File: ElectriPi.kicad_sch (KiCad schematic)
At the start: 56 parts, among them IC2 TPS51397ARJER, J1 282837-2, J2 JST XH 01x02, J3 JST XH 01x02, J6 Raspberry_Pi_2_3, J8 JST XH 01x02, Q1 SiA471DJ, Q2 SiA430DJT, U1 LM74700, U2 COOLING

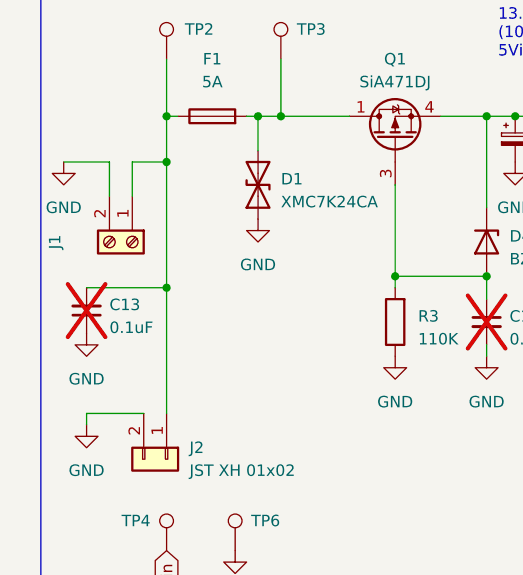
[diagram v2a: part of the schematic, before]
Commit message: Updated fuseholder to Keystone 3557 - low profile mini ATO fuses.
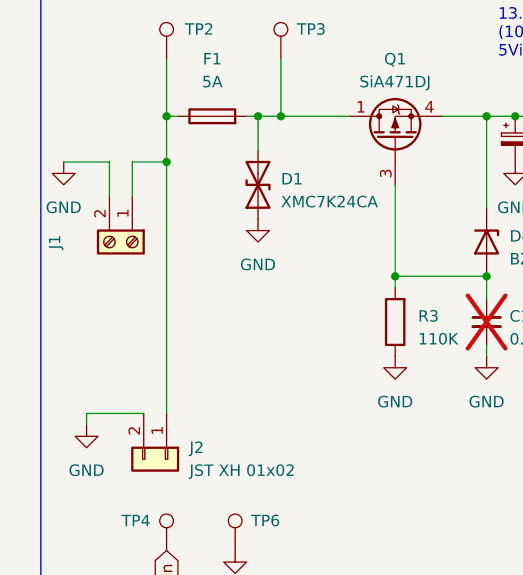
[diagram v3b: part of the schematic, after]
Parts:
- removed C13: 0.1uF, Capacitor_SMD:C_0402_1005Metric, symbol Device:C_Small
- F1: footprint Fuse:Fuse_Littelfuse-NANO2-451_453 -> Fuse:Fuseholder_Blade_Mini_Keystone_3557; DigiKey F1889-ND -> 36-3557-2-ND
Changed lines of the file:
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@@
   (junction (at 31.75 40.64) (diameter 0) (color 0 0 0 0)
-  )
-  (junction (at 31.75 59.69) (diameter 0) (color 0 0 0 0)
   )
   (junction (at 92.075 40.64) (diameter 0) (color 0 0 0 0)
@@
     (stroke (width 0) (type default))
   )
-  (wire (pts (xy 31.75 59.69) (xy 31.75 73.66))
-    (stroke (width 0) (type default))
-  )
   (wire (pts (xy 217.17 53.34) (xy 217.17 50.8))
     (stroke (width 0) (type default))
@@
     (stroke (width 0) (type default))
   )
-  (wire (pts (xy 22.86 59.69) (xy 31.75 59.69))
-    (stroke (width 0) (type default))
-  )
   (polyline (pts (xy 232.41 25.4) (xy 232.41 101.6))
     (stroke (width 0) (type default))
@@
     (stroke (width 0) (type default))
   )
-  (wire (pts (xy 31.75 45.72) (xy 31.75 59.69))
+  (wire (pts (xy 31.75 45.72) (xy 31.75 73.66))
     (stroke (width 0) (type default))
   )
@@
     )
   )
-  (symbol (lib_id "Device:C_Small") (at 22.86 62.23 180) (unit 1)
-    (in_bom yes) (on_board yes) (dnp yes) (fields_autoplaced)
-    (property "Reference" "C13" (at 25.4 61.5886 0)
-      (effects (font (size 1.27 1.27)) (justify right))
-    )
-    (property "Value" "0.1uF" (at 25.4 64.1286 0)
-      (effects (font (size 1.27 1.27)) (justify right))
-    )
-    (property "Footprint" "Capacitor_SMD:C_0402_1005Metric" (at 22.86 62.23 0)
-      (effects (font (size 1.27 1.27)) hide)
-    )
-    (property "Datasheet" "~" (at 22.86 62.23 0)
-      (effects (font (size 1.27 1.27)) hide)
-    )
-    (property "Mouser" "81-GRM155R62A104KE4J" (at 22.86 62.23 0)
-      (effects (font (size 1.27 1.27)) hide)
-    )
-    (property "LCSC" "C2193622" (at 22.86 62.23 0)
-      (effects (font (size 1.27 1.27)) hide)
-    )
-    (property "DigiKey" "490-GRM155R62A104KE14JTR-ND" (at 22.86 62.23 0)
-      (effects (font (size 1.27 1.27)) hide)
-    )
-    (pin "1")
-    (pin "2")
-    (instances
-      (project "ElectriPi"
-        (path "/e63e39d7-6ac0-4ffd-8aa3-1841a4541b55"
-          (reference "C13") (unit 1)
-        )
-      )
-    )
-  )
   (symbol (lib_id "power:PWR_FLAG") (at 217.17 138.43 0) (unit 1)
     (in_bom yes) (on_board yes) (dnp no) (fields_autoplaced)
@@
     )
   )
-  (symbol (lib_id "power:GND") (at 22.86 64.77 0) (unit 1)
-    (in_bom yes) (on_board yes) (dnp no) (fields_autoplaced)
-    (property "Reference" "#PWR043" (at 22.86 71.12 0)
-      (effects (font (size 1.27 1.27)) hide)
-    )
-    (property "Value" "GND" (at 22.86 69.85 0)
-      (effects (font (size 1.27 1.27)))
-    )
-    (property "Footprint" "" (at 22.86 64.77 0)
-      (effects (font (size 1.27 1.27)) hide)
-    )
-    (property "Datasheet" "" (at 22.86 64.77 0)
-      (effects (font (size 1.27 1.27)) hide)
-    )
-    (pin "1")
-    (instances
-      (project "ElectriPi"
-        (path "/e63e39d7-6ac0-4ffd-8aa3-1841a4541b55"
-          (reference "#PWR043") (unit 1)
-        )
-      )
-    )
-  )
   (symbol (lib_id "Connector:TestPoint") (at 39.37 88.9 0) (unit 1)
     (in_bom no) (on_board yes) (dnp no)
@@
       (effects (font (size 1.27 1.27)))
     )
-    (property "Footprint" "Fuse:Fuse_Littelfuse-NANO2-451_453" (at 36.83 42.418 90)
+    (property "Footprint" "Fuse:Fuseholder_Blade_Mini_Keystone_3557" (at 36.83 42.418 90)
       (effects (font (size 1.27 1.27)) hide)
     )
@@
       (effects (font (size 1.27 1.27)) hide)
     )
-    (property "DigiKey" "F1889-ND" (at 36.83 40.64 90)
-      (effects (font (size 1.27 1.27)) hide)
-    )
+    (property "DigiKey" "36-3557-2-ND" (at 36.83 40.64 90)
+      (effects (font (size 1.27 1.27)) hide)
+    )

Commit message: updated BOM, gerbers, and symbol fields (mouser and LCSC PNs updated, useless fields removed)
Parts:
- C3: ManfNum CL10A105KB8NNNC -> (none); Mouser (none) -> 187-CL10A105KB8NNNC; PCBway CL10A105KB8NNNC -> (none); abv.Footprint 0603 -> (none)
- D3, D5: ManfNum 19-213/Y2C-CQ2R2L/3T(CY) -> (none); Mouser (none) -> 604-APT1608SYCK; PCBway 19-213/Y2C-CQ2R2L/3T(CY) -> (none); abv.Footprint 0603 -> (none)
- F1: LCSC C108518 -> C352820; Mouser (none) -> 534-3557-2
- IC2: Arrow Part Number TPS51397ARJER -> (none); Arrow Price/Stock https://www.arrow.com/en/products/tps51397arjer/texas-instr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 -> (none); Height 1 -> (none); Manufacturer_Name Texas Instruments -> (none); Manufacturer_Part_Number TPS51397ARJER -> (none); Mouser (none) -> 595-TPS51397ARJER; Mouser Part Number 595-TPS51397ARJER -> (none); Mouser Price/Stock https://www.mouser.co.uk/ProductDetail/Texas-Instruments/TP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 -> (none)
- J1: LCSC (none) -> C592976; Mouser (none) -> 571-2828372
- J3, J8: DigiKey (none) -> 455-B2B-XH-A-ND
- R1, R11, R5: Mouser (none) -> 652-CR0402FX-3302GLF
- R12, R13, R3, R7: Mouser (none) -> 652-CR0402FX-1103GLF
- R14: Mouser (none) -> 652-CR0402FX-1502GLF
- R4: Mouser (none) -> 652-CR0402FX-1803GLF
- R6: ManfNum 0402WGF2000TCE -> (none); Mouser (none) -> 603-RC0402FR-071KL; PCBway 0402WGF2000TCE -> (none); abv.Footprint 0402 -> (none)
- R8: ManfNum 0402WGF1501TCE -> (none); Mouser (none) -> 652-CR0402FX-1002GLF; PCBway 0402WGF1501TCE -> (none); abv.Footprint 0402 -> (none)

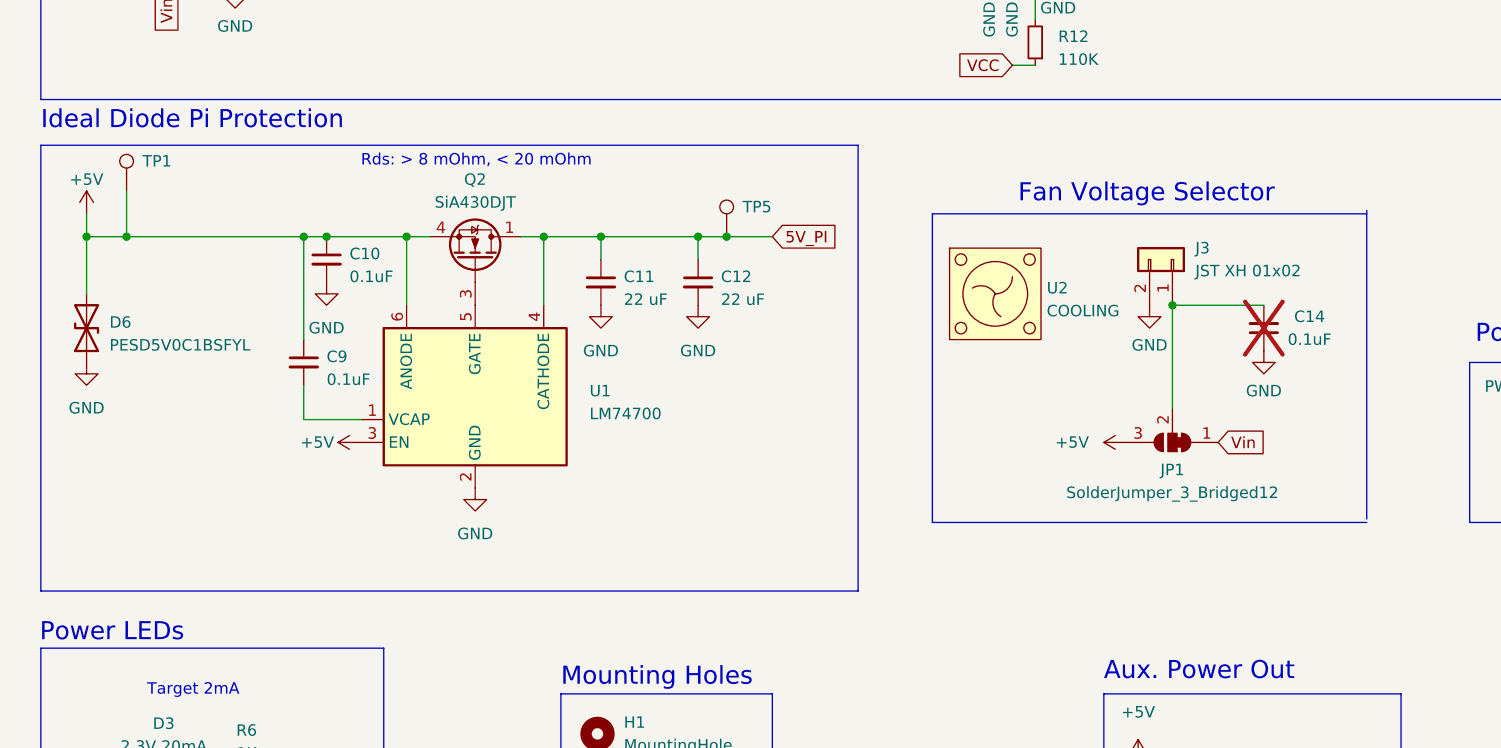
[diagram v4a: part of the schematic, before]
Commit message: update to new output surge/TVS protection suitable for DC supply. Still require manf output and bom regeneration.
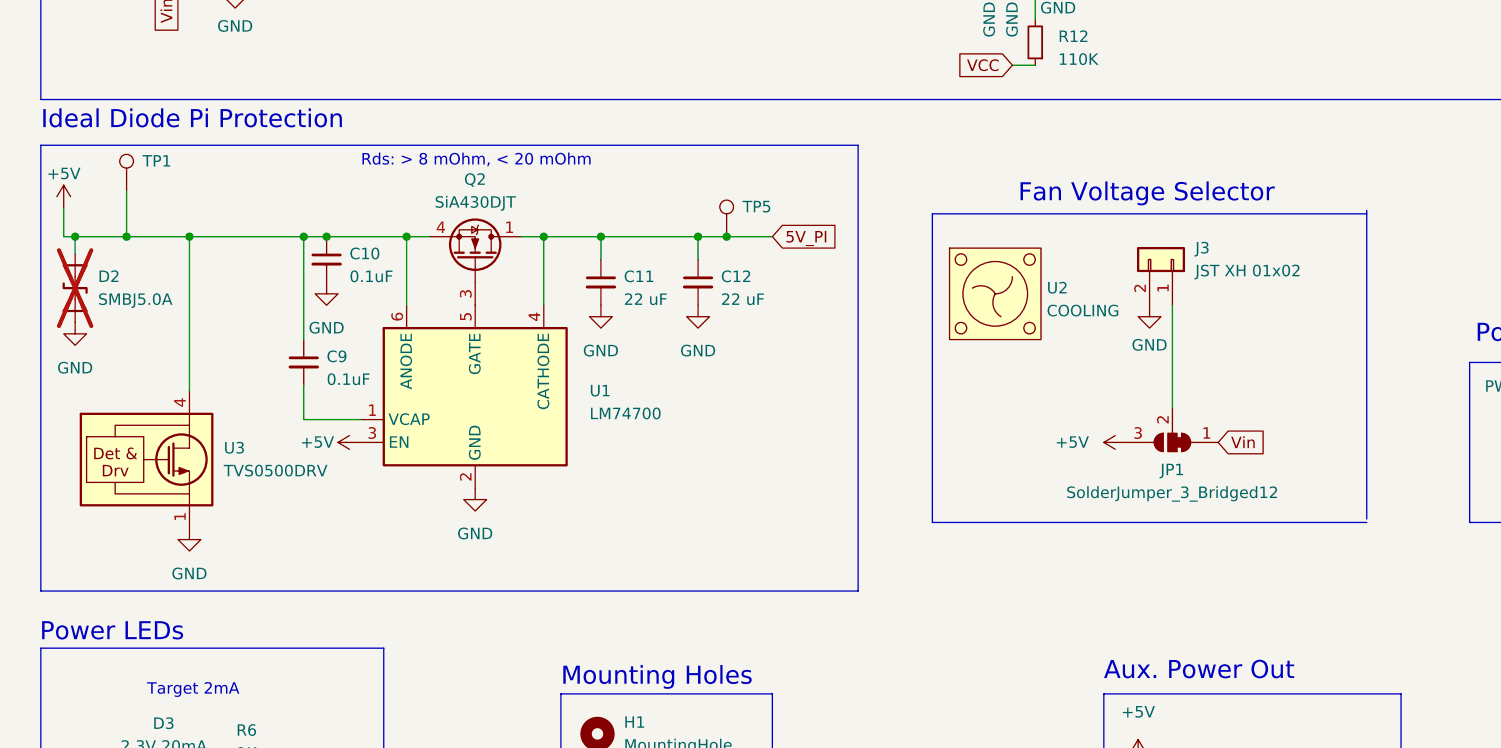
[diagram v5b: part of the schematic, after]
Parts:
- removed C14: 0.1uF, Capacitor_SMD:C_0402_1005Metric, symbol Device:C_Small
- removed D6: PESD5V0C1BSFYL, Diode_SMD:Nexperia_DSN0603-2_0.6x0.3mm_P0.4mm, symbol Device:D_TVS
- added D2: SMBJ5.0A, Diode_SMD:D_SMB, symbol Device:D_TVS
- added U3: TVS0500DRV, Package_SON:WSON-6-1EP_2x2mm_P0.65mm_EP1x1.6mm, symbol Power_Protection:TVS0500DRV
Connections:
- net +5V: now also D2.2 (A2), U3.4 (IN), U3.5 (IN), U3.6 (IN)
- net GND: now also D2.1 (A1), U3.1 (GND), U3.2 (GND), U3.3 (GND), U3.7 (GND)

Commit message: hide fan from BOM
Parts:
- U2: now left out of the parts list
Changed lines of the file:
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@@
   )
   (symbol (lib_id "FAN:COOLING") (at 123.825 123.19 0) (unit 1)
-    (in_bom yes) (on_board yes) (dnp no) (fields_autoplaced)
+    (in_bom no) (on_board yes) (dnp no) (fields_autoplaced)
     (property "Reference" "U2" (at 129.54 122.555 0)
       (effects (font (size 1.27 1.27)) (justify left))

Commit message: Add BOM exclusions for THT and DNP
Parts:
- C15, C17, D2, F1, J2, J8: now left out of the parts list
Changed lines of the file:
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@@
   )
   (symbol (lib_id "Device:C_Small") (at 67.31 63.5 0) (unit 1)
-    (in_bom yes) (on_board yes) (dnp yes) (fields_autoplaced)
+    (in_bom no) (on_board yes) (dnp yes) (fields_autoplaced)
     (property "Reference" "C17" (at 69.85 62.8713 0)
       (effects (font (size 1.27 1.27)) (justify left))
@@
   )
   (symbol (lib_id "Device:C_Small") (at 139.7 177.8 0) (unit 1)
-    (in_bom yes) (on_board yes) (dnp yes) (fields_autoplaced)
+    (in_bom no) (on_board yes) (dnp yes) (fields_autoplaced)
     (property "Reference" "C15" (at 142.24 177.1713 0)
       (effects (font (size 1.27 1.27)) (justify left))
@@
   )
   (symbol (lib_id "Connector_Generic:Conn_01x02") (at 31.75 78.74 270) (unit 1)
-    (in_bom yes) (on_board yes) (dnp no) (fields_autoplaced)
+    (in_bom no) (on_board yes) (dnp no) (fields_autoplaced)
     (property "Reference" "J2" (at 34.29 77.4699 90)
       (effects (font (size 1.27 1.27)) (justify left))
@@
   )
   (symbol (lib_id "Device:Fuse") (at 36.83 40.64 90) (unit 1)
-    (in_bom yes) (on_board yes) (dnp no) (fields_autoplaced)
+    (in_bom no) (on_board yes) (dnp no) (fields_autoplaced)
     (property "Reference" "F1" (at 36.83 34.29 90)
       (effects (font (size 1.27 1.27)))
@@
   )
   (symbol (lib_id "Device:D_TVS") (at 21.59 122.555 90) (unit 1)
-    (in_bom yes) (on_board yes) (dnp yes) (fields_autoplaced)
+    (in_bom no) (on_board yes) (dnp yes) (fields_autoplaced)
     (property "Reference" "D2" (at 24.13 121.285 90)
       (effects (font (size 1.27 1.27)) (justify right))
@@
   )
   (symbol (lib_id "Connector_Generic:Conn_01x02") (at 161.29 176.53 0) (unit 1)
-    (in_bom yes) (on_board yes) (dnp no)
+    (in_bom no) (on_board yes) (dnp no)
     (property "Reference" "J8" (at 161.29 185.1152 0)
       (effects (font (size 1.27 1.27)))

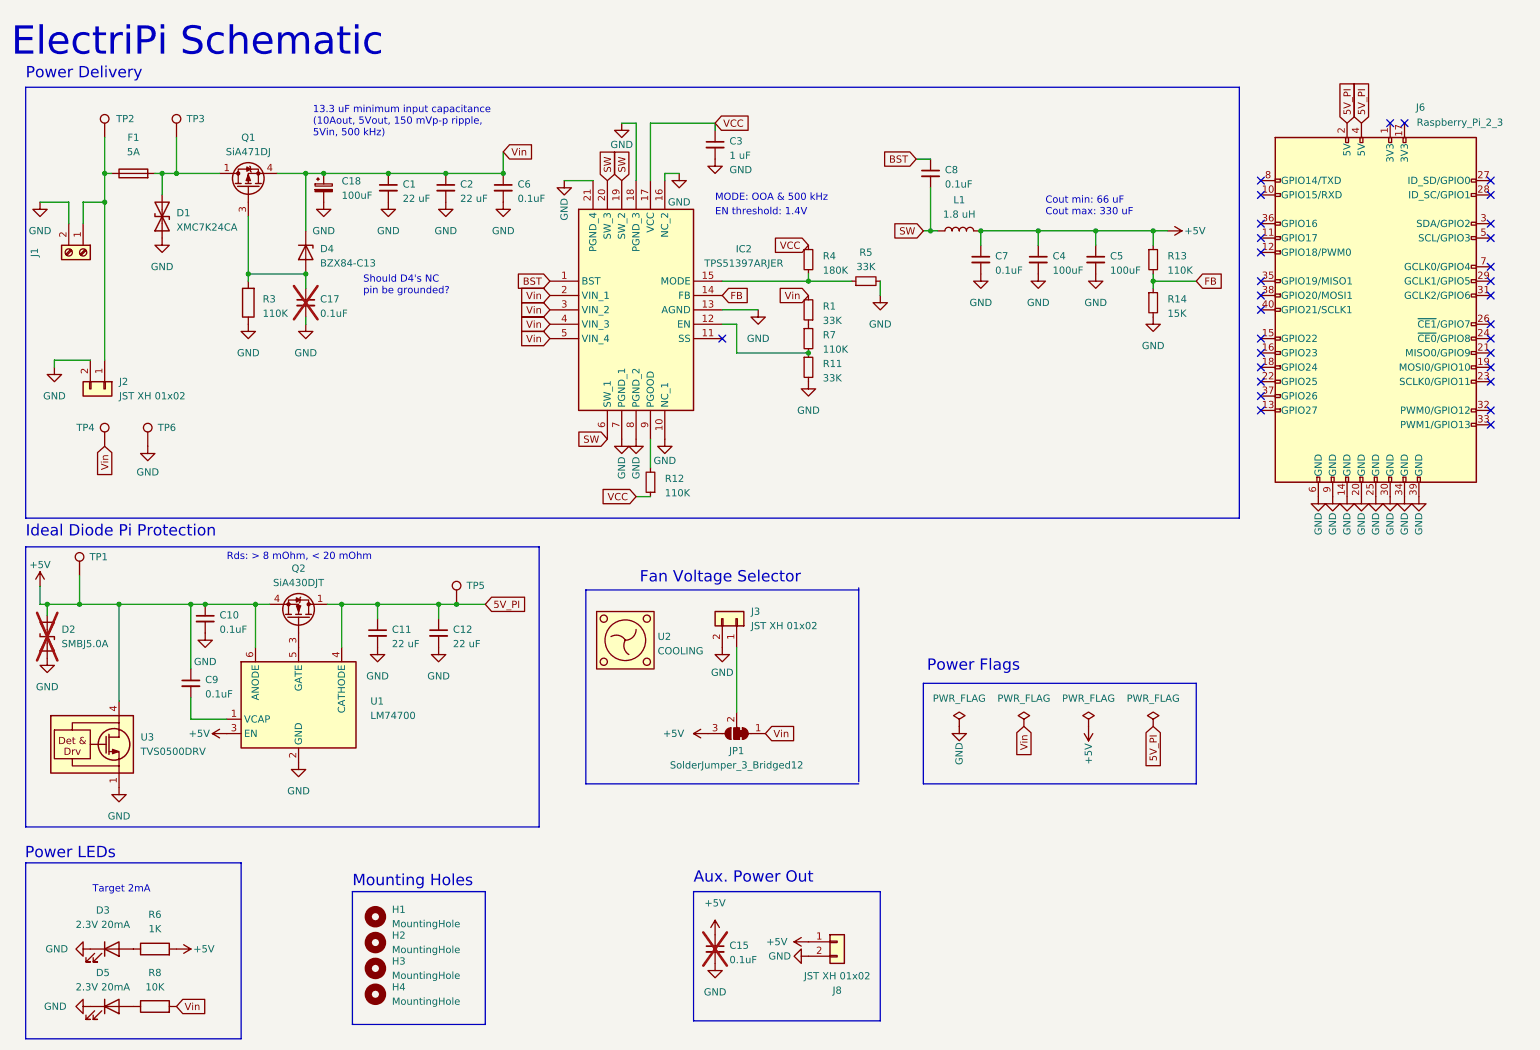
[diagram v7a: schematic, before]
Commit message: Remove JST input / output connectors! Not rated for currents
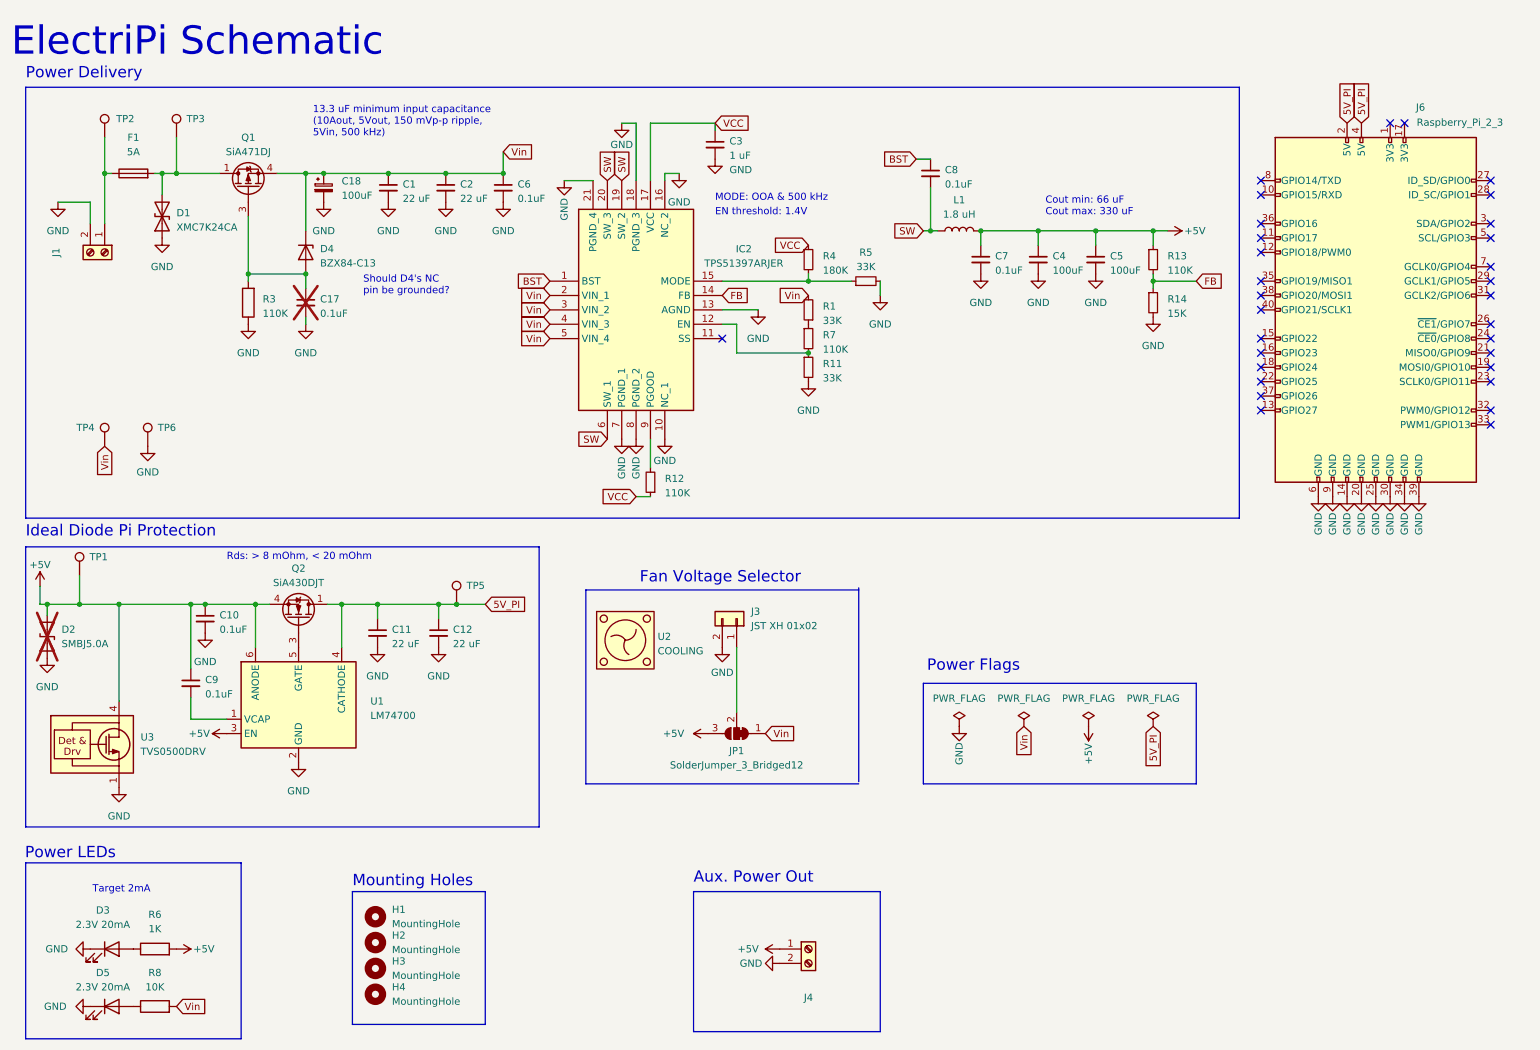
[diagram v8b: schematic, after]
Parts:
- removed C15: 0.1uF, Capacitor_SMD:C_0402_1005Metric, symbol Device:C_Small
- removed J2, J8: JST XH 01x02, Connector_JST:JST_XH_B2B-XH-A_1x02_P2.50mm_Vertical, symbol Connector_Generic:Conn_01x02
- added J4: 282837-2, TerminalBlock:TerminalBlock_bornier-2_P5.08mm, symbol Connector:Screw_Terminal_01x02
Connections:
- net +5V: now also J4.1 (Pin_1)
- net GND: now also J4.2 (Pin_2)
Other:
- moved on the sheet: J1
